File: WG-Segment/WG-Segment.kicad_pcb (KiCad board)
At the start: 4 copper layers, 100 x 100 mm, 137 parts, among them J101 Conn_01x02, J102 Conn_02x04_Odd_Even, J201 Conn_01x03, J202 Conn_01x02, J203 Conn_01x04, J501 Conn_01x02, J502 Conn_01x02, J503 Conn_01x02, J504 Conn_01x02, J505 Conn_01x02, J506 Conn_01x02, J507 Conn_01x02, J508 Conn_01x02, J509 Conn_01x02, J510 Conn_01x02, J511 Conn_01x02, J512 Conn_01x02, J513 Conn_01x02, J514 Conn_01x02, J515 Conn_01x02, J516 Conn_01x02, J517 Conn_01x02, J518 Conn_01x02, J519 Conn_01x02, J520 Conn_01x02, J521 Conn_01x02, J522 Conn_01x02, J523 Conn_01x02, J524 Conn_01x02, J525 Conn_01x02, SW201 SPST-NO, U201 W25Q16JV, U202 RP2040, U301 AP63205WU, U302 MIC5504-3.3YM5, U303 MCP1501T-33E, U401 SN74LV1T34DCK, U501 SN74LV4051ADYYR, U502 SN74LV4051ADYYR, U503 SN74LV4051ADYYR, U504 SN74LV4051ADYYR, Y201 12MHz

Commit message: Fix build issues
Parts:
- C201, C202, C205, C206, C207, C208, C209, C210, C211, C212, C213, C301, C501, C502, C503, C504: value 100n -> 0.1u
- C305, C306: value 1u/10V -> 1u,10V
- R501, R502, R503, R504: value 22k/0.1% -> 22k,0.1%
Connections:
- net Net-(J202-Pin_1) renamed /CPU/~{USB_BOOT}

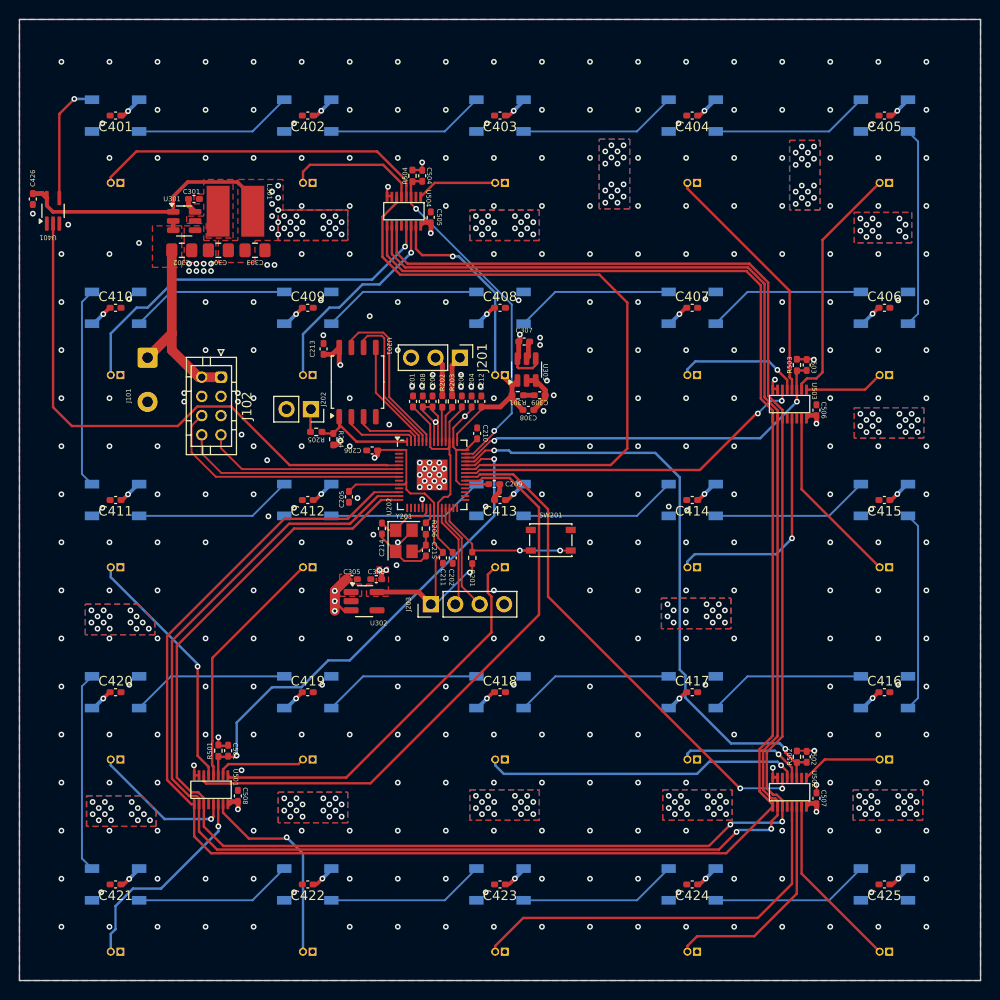
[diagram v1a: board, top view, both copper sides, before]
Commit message: Add tolerances and dimensions
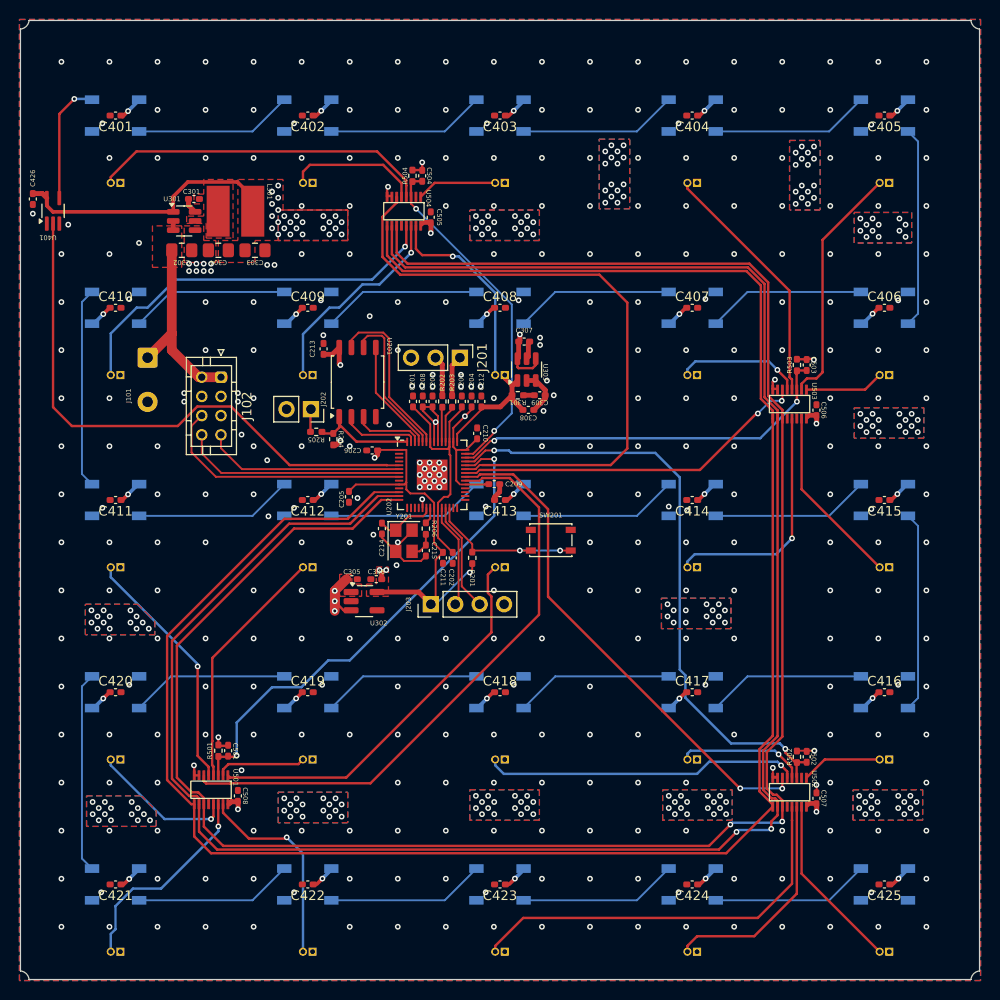
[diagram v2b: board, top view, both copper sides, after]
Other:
- board size 100 x 100 mm -> 99.8 x 99.8 mm
- board text added: "Arc radius:"
- board text added: "Edge tolerance:"
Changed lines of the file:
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@@
     (pad_to_mask_clearance 0)
     (aux_axis_origin 97.16 48.12)
+    (grid_origin 97.16 48.12)
     (pcbplotparams
       (layerselection 0x00010fc_ffffffff)
@@
   (gr_rect (start 117.635 68.595) (end 136.685 87.645)
     (stroke (width 0.1) (type default)) (fill none) (layer "B.SilkS"))
+  (gr_rect (start 97.26 48.22) (end 197.06 148.02)
+    (stroke (width 0.05) (type default)) (fill none) (layer "Dwgs.User"))
   (gr_rect (start 97.16 48.12) (end 197.16 148.12)
-    (stroke (width 0.05) (type default)) (fill none) (layer "Edge.Cuts"))
+    (stroke (width 0.05) (type default)) (fill none) (layer "Dwgs.User"))
+  (gr_line (start 98.16 48.2216) (end 196.16 48.2216)
+    (stroke (width 0.05) (type default)) (layer "Edge.Cuts"))
+  (gr_arc (start 97.2616 147.12) (mid 97.870747 147.409253) (end 98.16 148.0184)
+    (stroke (width 0.05) (type default)) (layer "Edge.Cuts"))
+  (gr_line (start 97.2616 147.12) (end 97.2616 49.12)
+    (stroke (width 0.05) (type default)) (layer "Edge.Cuts"))
+  (gr_arc (start 98.16 48.2216) (mid 97.870747 48.830747) (end 97.2616 49.12)
+    (stroke (width 0.05) (type default)) (layer "Edge.Cuts"))
+  (gr_arc (start 197.0584 49.12) (mid 196.449253 48.830747) (end 196.16 48.2216)
+    (stroke (width 0.05) (type default)) (layer "Edge.Cuts"))
+  (gr_line (start 196.16 148.0184) (end 98.16 148.0184)
+    (stroke (width 0.05) (type default)) (layer "Edge.Cuts"))
+  (gr_arc (start 196.16 148.0184) (mid 196.449253 147.409253) (end 197.0584 147.12)
+    (stroke (width 0.05) (type default)) (layer "Edge.Cuts"))
+  (gr_line (start 197.0584 49.12) (end 197.0584 147.12)
+    (stroke (width 0.05) (type default)) (layer "Edge.Cuts"))
+  (gr_text "Arc radius:" (at 93.16 151.12 90) (layer "Cmts.User")
+    (effects (font (size 0.25 0.25) (thickness 0.0375)) (justify left bottom))
+  )
+  (gr_text "Edge tolerance:" (at 193.16 151.12) (layer "Cmts.User")
+    (effects (font (size 0.25 0.25) (thickness 0.0375)) (justify left bottom))
+  )
+  (dimension (type aligned) (layer "Cmts.User")
+    (pts (xy 156.685 147.645) (xy 157.635 147.645))
+    (height 3.475)
+    (gr_text "0.9500 mm" (at 157.16 152.12) (layer "Cmts.User")
+      (effects (font (size 1 1) (thickness 0.15)))
+    )
+    (format (prefix "") (suffix "") (units 2) (units_format 1) (precision 4))
+    (style (thickness 0.1) (arrow_length 0.3175) (text_position_mode 2) (extension_height 0.58642) (extension_offset 0.5) keep_text_aligned)
+  )
+  (dimension (type aligned) (layer "Cmts.User")
+    (pts (xy 97.155 48.133) (xy 197.155 48.133))
+    (height -2.013)
+    (gr_text "100.0000 mm" (at 147.155 44.97) (layer "Cmts.User")
+      (effects (font (size 1 1) (thickness 0.15)))
+    )
+    (format (prefix "") (suffix "") (units 2) (units_format 1) (precision 4))
+    (style (thickness 0.1) (arrow_length 1.27) (text_position_mode 0) (extension_height 0.58642) (extension_offset 0.5) keep_text_aligned)
+  )
+  (dimension (type aligned) (layer "Cmts.User")
+    (pts (xy 117.635 147.645) (xy 136.685 147.645))
+    (height 3.474999)
+    (gr_text "19.0500 mm" (at 127.16 152.12) (layer "Cmts.User")
+      (effects (font (size 1 1) (thickness 0.15)))
+    )
+    (format (prefix "") (suffix "") (units 2) (units_format 1) (precision 4))
+    (style (thickness 0.1) (arrow_length 1.27) (text_position_mode 2) (extension_height 0.58642) (extension_offset 0.5) keep_text_aligned)
+  )
+  (dimension (type aligned) (layer "Cmts.User")
+    (pts (xy 197.16 48.12) (xy 197.16 148.12))
+    (height -3)
+    (gr_text "100.0000 mm" (at 199.01 98.12 90) (layer "Cmts.User")
+      (effects (font (size 1 1) (thickness 0.15)))
+    )
+    (format (prefix "") (suffix "") (units 2) (units_format 1) (precision 4))
+    (style (thickness 0.1) (arrow_length 1.27) (text_position_mode 0) (extension_height 0.58642) (extension_offset 0.5) keep_text_aligned)
+  )
+  (dimension (type orthogonal) (layer "Cmts.User")
+    (pts (xy 97.16 148.12) (xy 97.2616 147.12))
+    (height -2)
+    (orientation 1)
+    (gr_text "1.0000 mm" (at 94.01 147.12 90) (layer "Cmts.User")
+      (effects (font (size 1 1) (thickness 0.15)))
+    )
+    (format (prefix "") (suffix "") (units 2) (units_format 1) (precision 4))
+    (style (thickness 0.1) (arrow_length 0.3175) (text_position_mode 2) (extension_height 0.58642) (extension_offset 0.5) keep_text_aligned)
+  )
+  (dimension (type orthogonal) (layer "Cmts.User")
+    (pts (xy 97.635 147.645) (xy 97.16 148.12))
+    (height 3.475)
+    (orientation 0)
+    (gr_text "0.4750 mm" (at 98.16 152.12) (layer "Cmts.User")
+      (effects (font (size 1 1) (thickness 0.15)))
+    )
+    (format (prefix "") (suffix "") (units 2) (units_format 1) (precision 4))
+    (style (thickness 0.1) (arrow_length 0.3175) (text_position_mode 2) (extension_height 0.58642) (extension_offset 0.5) keep_text_aligned)
+  )
+  (dimension (type orthogonal) (layer "Cmts.User")
+    (pts (xy 197.06 148.02) (xy 197.16 148.12))
+    (height 3.1)
+    (orientation 0)
+    (gr_text "0.1000 mm" (at 197.16 152.12) (layer "Cmts.User")
+      (effects (font (size 1 1) (thickness 0.15)))
+    )
+    (format (prefix "") (suffix "") (units 2) (units_format 1) (precision 4))
+    (style (thickness 0.1) (arrow_length 0.3175) (text_position_mode 2) (extension_height 0.58642) (extension_offset 0.5) keep_text_aligned)
+  )
   (segment (start 139.902 92.07) (end 139.902 90.2275) (width 0.2) (layer "F.Cu") (net 1))
   (segment (start 140.10564 92.8075) (end 141.69836 92.8075) (width 0.2) (layer "F.Cu") (net 1))

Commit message: Update parts to ones in JLCPCB library
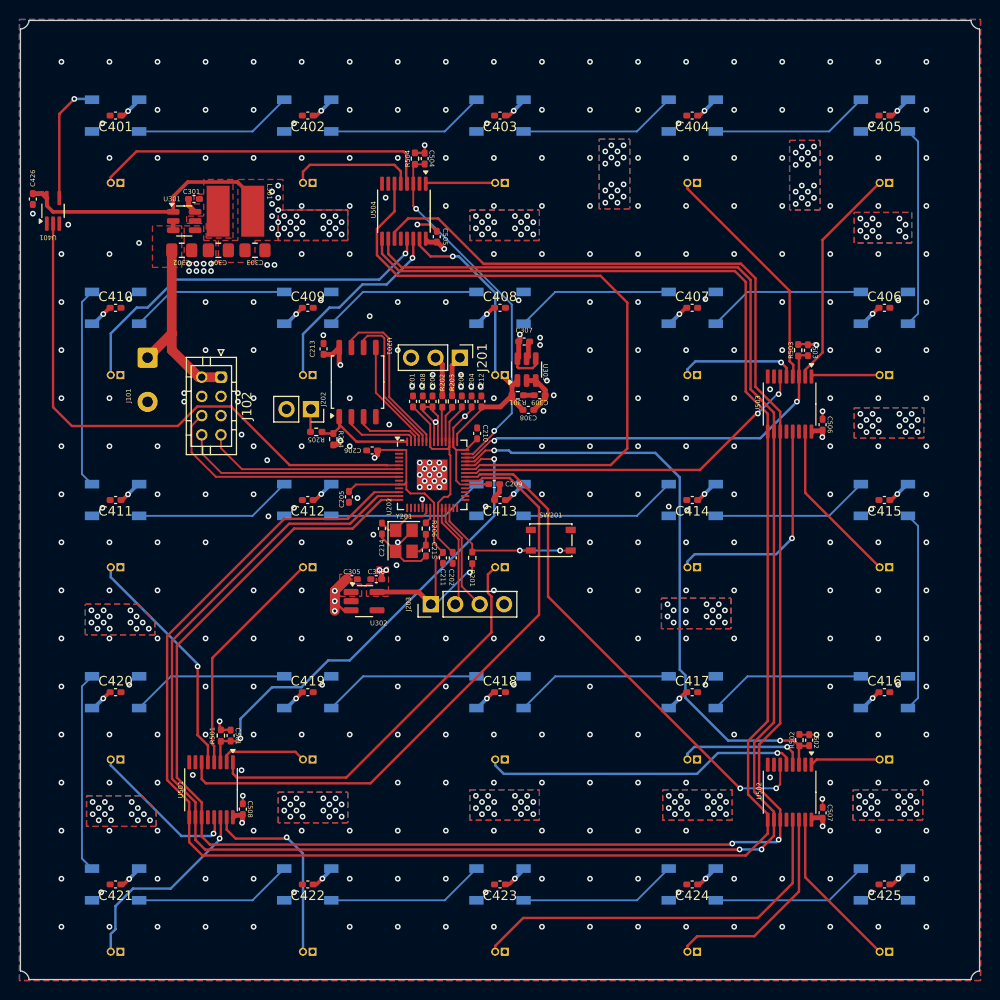
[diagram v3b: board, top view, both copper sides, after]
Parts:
- C305, C306: value 1u,10V -> 1u/10V
- R501, R502, R503, R504: value 22k,0.1% -> 22k/0.1%
- U501, U502, U503, U504: value SN74LV4051ADYYR -> SN74LV4051A; footprint WordGameLib:SOT-23-THIN-16 -> Package_SO:TSSOP-16_4.4x5mm_P0.65mm
- moved C505 2.11 mm to (140.6, 70.7)
- moved C504 1.81 mm to (139.3, 62.6)
- moved R504 1.81 mm to (138.3, 62.6)
- moved C502 1.75 mm to (179.3, 123.1)
- moved R502 1.75 mm to (178.3, 123.1)
- moved C506 1.64 mm to (180.7, 90.3)
- moved C507 1.64 mm to (180.7, 130.7)
- moved C501 1.60 mm to (119.1, 122.6)
- moved R501 1.60 mm to (118.1, 122.6)
- moved C503 1.54 mm to (179.2, 82.5)
- moved R503 1.54 mm to (178.2, 82.5)
- moved C508 1.48 mm to (120.4, 130.3)
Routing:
- net GND: track 33.3 -> 30.3 mm, vias 358 -> 360
- net /Tile Connector/A5: track 25.5 -> 23.4 mm
- net /Tile Connector/A8: track 21.1 -> 19.2 mm
- net /CPU/ADC2: track 40.9 -> 42.7 mm
- net /CPU/ADC3: track 35.9 -> 37.7 mm
- net /Tile Connector/A25: track 18.5 -> 16.9 mm
- net /Tile Connector/A15: track 18.8 -> 17.3 mm
- net /CPU/ADC0: track 52.0 -> 50.6 mm
- net /CPU/MUX_~{EN}_1: track 63.1 -> 64.5 mm
- net /Tile Connector/A11: track 25.9 -> 24.5 mm
- net /Tile Connector/A12: track 25.6 -> 24.3 mm
- net /Tile Connector/A23: track 42.2 -> 40.9 mm
- net /Tile Connector/A14: track 25.0 -> 23.6 mm
- net /CPU/MUX_~{EN}_4: track 67.9 -> 69.2 mm
- net /Tile Connector/A24: track 23.3 -> 22.0 mm
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
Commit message: Update regulator
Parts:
- removed C309: 2.2u, Capacitor_SMD:C_0402_1005Metric_Pad0.74x0.62mm_HandSolder
- added D301: SS34, Diode_SMD:D_SMA, F.Cu at (112.8, 77.7)
- added D302: RED, LED_SMD:LED_0603_1608Metric_Pad1.05x0.95mm_HandSolder, F.Cu at (119.4, 144.3)
- added R302: 30k, Resistor_SMD:R_0402_1005Metric_Pad0.72x0.64mm_HandSolder, F.Cu at (113.0, 66.8)
- added R303: 470R, Resistor_SMD:R_0402_1005Metric_Pad0.72x0.64mm_HandSolder, F.Cu at (116.5, 144.3)
- C307: value 2.2u -> 470n
- C308: value 1n -> 100p
- L301: value 4.7uH -> 10uH; footprint WordGameLib:Murata_1255AY -> WordGameLib:Murata_6060
- R301: value 50R -> 157k
- R501, R502, R503, R504: value 22k/0.1% -> 8k2/0.1%
- U301: value AP63205WU -> AP63200WU
- U303: value MCP1501T-33E -> REF3033; footprint Package_TO_SOT_SMD:SOT-23-6 -> Package_TO_SOT_SMD:SOT-23
- moved C308 45.1 mm to (110.4, 67.4), turned to 90 degrees
- moved R301 42.5 mm to (111.4, 67.4), turned to 90 degrees
- moved C307 2.06 mm to (150.9, 83.3)
- moved U303 1.25 mm to (150.2, 85.8), turned to -90 degrees
- moved C302 0.11 mm to (114.1, 72.2)
- moved C303 0.11 mm to (121.7, 72.2)
- moved C304 0.11 mm to (117.9, 72.2)
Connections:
- C302 pad 1: +12V -> /Power/+12_IN
- C308 pad 1: GND -> +5V
- C308 pad 2: VREF -> Net-(U301-FB)
- R301 pad 1: VREF -> +5V
- R301 pad 2: Net-(C309-Pad1) -> Net-(U301-FB)
- U301 pad 1: +5V -> Net-(U301-FB)
- U301 pad 2: +12V -> /Power/+12_IN
- U301 pad 3: +12V -> /Power/+12_IN
- U303 pad 1: VREF -> +5V
- U303 pad 2: GND -> VREF
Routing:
- net +5V: track 102.2 -> 78.6 mm, vias 240 -> 247
- net +12V: track 21.4 -> 11.8 mm
- net Net-(U301-FB): track 0.00 -> 3.65 mm
- net GND: track 30.3 -> 32.5 mm
- net Net-(D302-K): track 0.00 -> 1.45 mm
- net VREF: track 739.3 -> 738.0 mm
- net Net-(C309-Pad1): track 1.12 -> 0.00 mm
- net /Power/+12_IN: track 0.00 -> 0.95 mm
- added copper zone on F.Cu, net /Power/+12_IN
- removed copper zone on F.Cu, net +12V
